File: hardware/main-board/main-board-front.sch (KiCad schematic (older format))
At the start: 25 parts, among them J5 Meter Probe, J6 Footswitch, J7 USB_A, Q1 BSS138, Q2 BSS138, Q3 BSS138, U10 USBLC6-2SC6, U11 STMPS2141, U12 USBLC6-2SC6, U9 P82B96

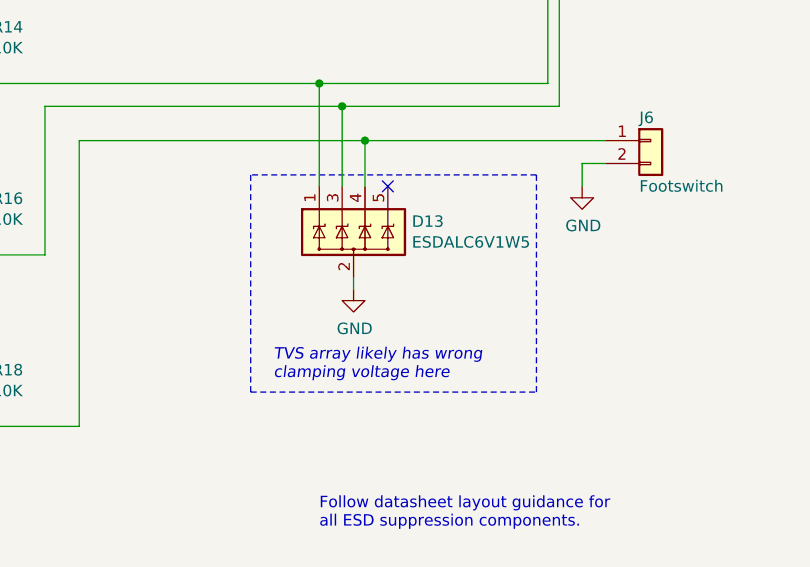
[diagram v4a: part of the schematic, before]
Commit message: Changed TVS protection on misc 5V front panel inputs
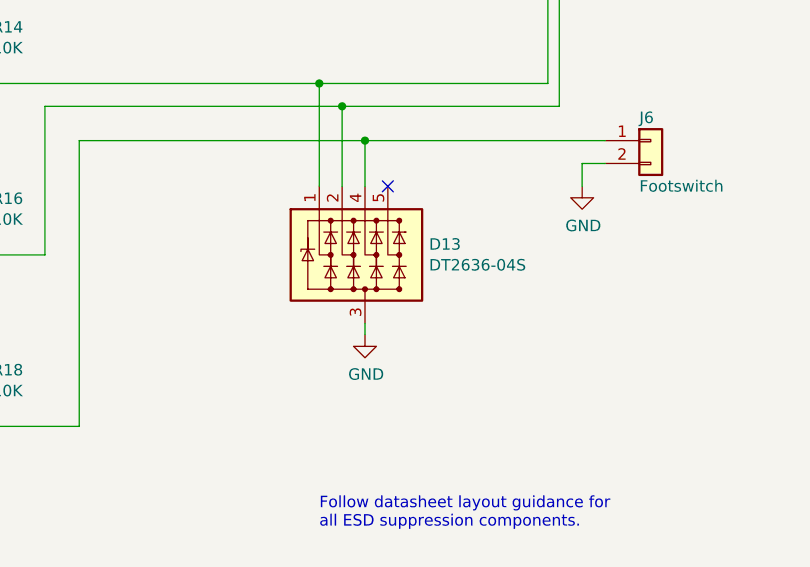
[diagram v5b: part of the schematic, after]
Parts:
- removed D13: ESDALC6V1W5, lib_fp:SOT323-5L, symbol Project:ESDALC6V1W5
- added D13: DT2636-04S, Package_TO_SOT_SMD:SOT-363_SC-70-6, symbol Project:DT2636-04S
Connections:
- net GND: now also D13.3 (GND)
- net at J6.1 (Pin_1), Q3.3 (D), R18.2: now also D13.4 (CH3)
- net at J5.6, Q1.3 (D), R14.2: now also D13.1 (CH1)
- net at J5.2, Q2.3 (D), R16.2: now also D13.2 (CH2)
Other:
- note removed: "TVS array likely has wrong\nclamping voltage here"
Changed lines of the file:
@@
 Connection ~ 2800 4150
-$Comp
-L Project:ESDALC6V1W5 D13
-U 1 1 5F9DF2EA
-P 5150 3300
-F 0 "D13" V 5104 3555 50  0000 L CNN
-F 1 "ESDALC6V1W5" V 5195 3555 50  0000 L CNN
-F 2 "lib_fp:SOT323-5L" H 5150 2925 50  0001 C CNN
-F 3 "https://www.st.com/content/ccc/resource/technical/document/datasheet/32/30/02/e6/ac/0f/46/c2/CD00002946.pdf/files/CD00002946.pdf/jcr:content/translations/en.CD00002946.pdf" H 5150 3350 50  0001 C CNN
-F 4 "TVS DIODE 3V SOT323-5" H 5150 3300 50  0001 C CNN "Description"
-F 5 "STMicroelectronics" H 5150 3300 50  0001 C CNN "Manufacturer"
-F 6 "ESDALC6V1W5" H 5150 3300 50  0001 C CNN "Manufacturer PN"
-F 7 "Digi-Key" H 5150 3300 50  0001 C CNN "Supplier"
-F 8 "497-7231-1-ND" H 5150 3300 50  0001 C CNN "Supplier PN"
-	1    5150 3300
-	0    1    1    0
-$EndComp
 $Comp
 L Power_Protection:USBLC6-2SC6 U?
@@
 L power:GND #PWR?
 U 1 1 5FA61E9F
-P 5150 3550
+P 5200 3750
 AR Path="/5FA61E9F" Ref="#PWR?"  Part="1"
 AR Path="/5FA19AFF/5FA61E9F" Ref="#PWR072"  Part="1"
-F 0 "#PWR072" H 5150 3300 50  0001 C CNN
-F 1 "GND" H 5155 3377 50  0000 C CNN
-F 2 "" H 5150 3550 50  0001 C CNN
-F 3 "" H 5150 3550 50  0001 C CNN
-	1    5150 3550
+F 0 "#PWR072" H 5200 3500 50  0001 C CNN
+F 1 "GND" H 5205 3577 50  0000 C CNN
+F 2 "" H 5200 3750 50  0001 C CNN
+F 3 "" H 5200 3750 50  0001 C CNN
+	1    5200 3750
 	1    0    0    -1
 $EndComp
 Wire Wire Line
-	5150 3500 5150 3550
+	5200 3700 5200 3750
 Text HLabel 1350 1450 0    50   BiDi ~ 0
 EXT_I2C_SDA
@@
 Wire Notes Line style solid
 	7700 1175 7700 1850
-Text Notes 4800 3950 0    50   Italic 0
-TVS array likely has wrong\nclamping voltage here
-Wire Notes Line
-	4700 3050 4700 4000
-Wire Notes Line
-	4700 4000 5950 4000
-Wire Notes Line
-	5950 4000 5950 3050
-Wire Notes Line
-	5950 3050 4700 3050
+$Comp
+L Project:DT2636-04S D13
+U 1 1 5FAA8A21
+P 5200 3400
+F 0 "D13" H 5480 3446 50  0000 L CNN
+F 1 "DT2636-04S" H 5480 3355 50  0000 L CNN
+F 2 "Package_TO_SOT_SMD:SOT-363_SC-70-6" H 5500 3350 50  0001 L CNN
+F 3 "https://www.diodes.com/assets/Datasheets/DT2636-04S.pdf" H 5525 3075 50  0001 C CNN
+F 4 "TVS DIODE 5.5V 9V SOT363" H 5200 3400 50  0001 C CNN "Description"
+F 5 "Diodes Incorporated" H 5200 3400 50  0001 C CNN "Manufacturer"
+F 6 "DT2636-04S-7" H 5200 3400 50  0001 C CNN "Manufacturer PN"
+F 7 "Digi-Key" H 5200 3400 50  0001 C CNN "Supplier"
+F 8 "DT2636-04S-7DICT-ND" H 5200 3400 50  0001 C CNN "Supplier PN"
+	1    5200 3400
+	1    0    0    -1
+$EndComp
 $EndSCHEMATC

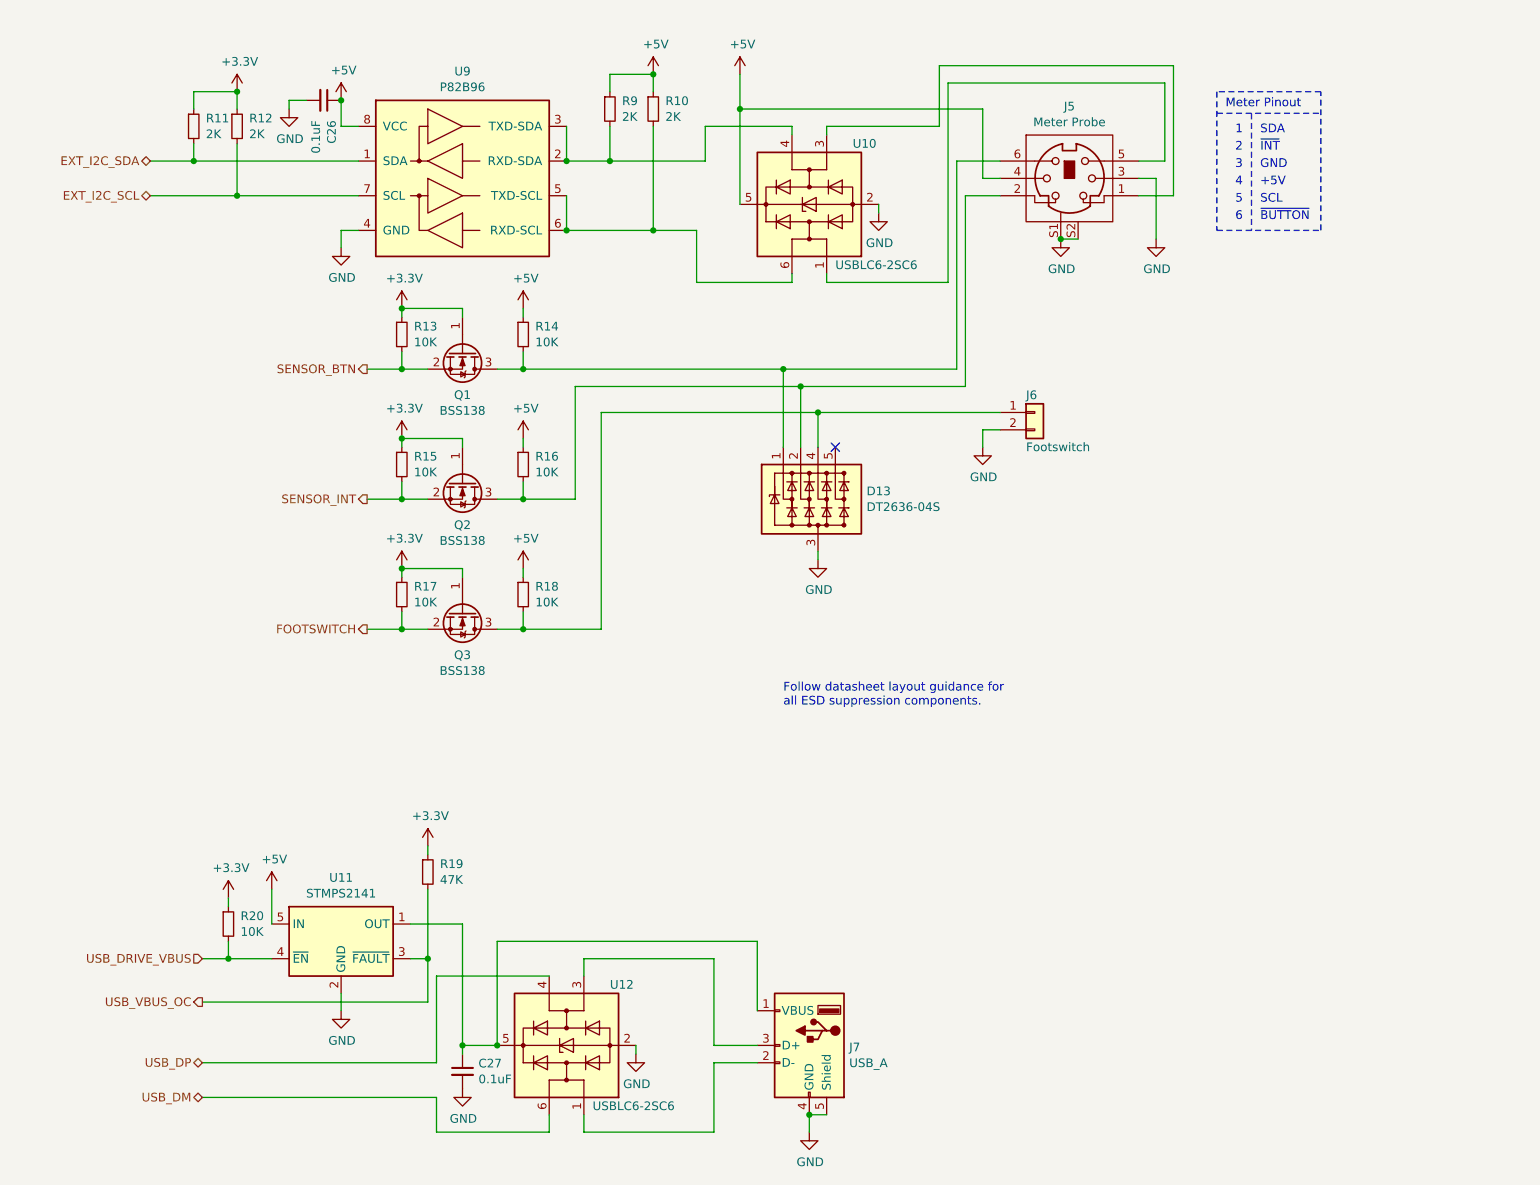
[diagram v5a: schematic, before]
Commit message: Main board schematic cleanup pass
Added mounting holes for the board and the OLED module
Connected GND and Earth nets
Cleaned up and labeled many parts of the schematic
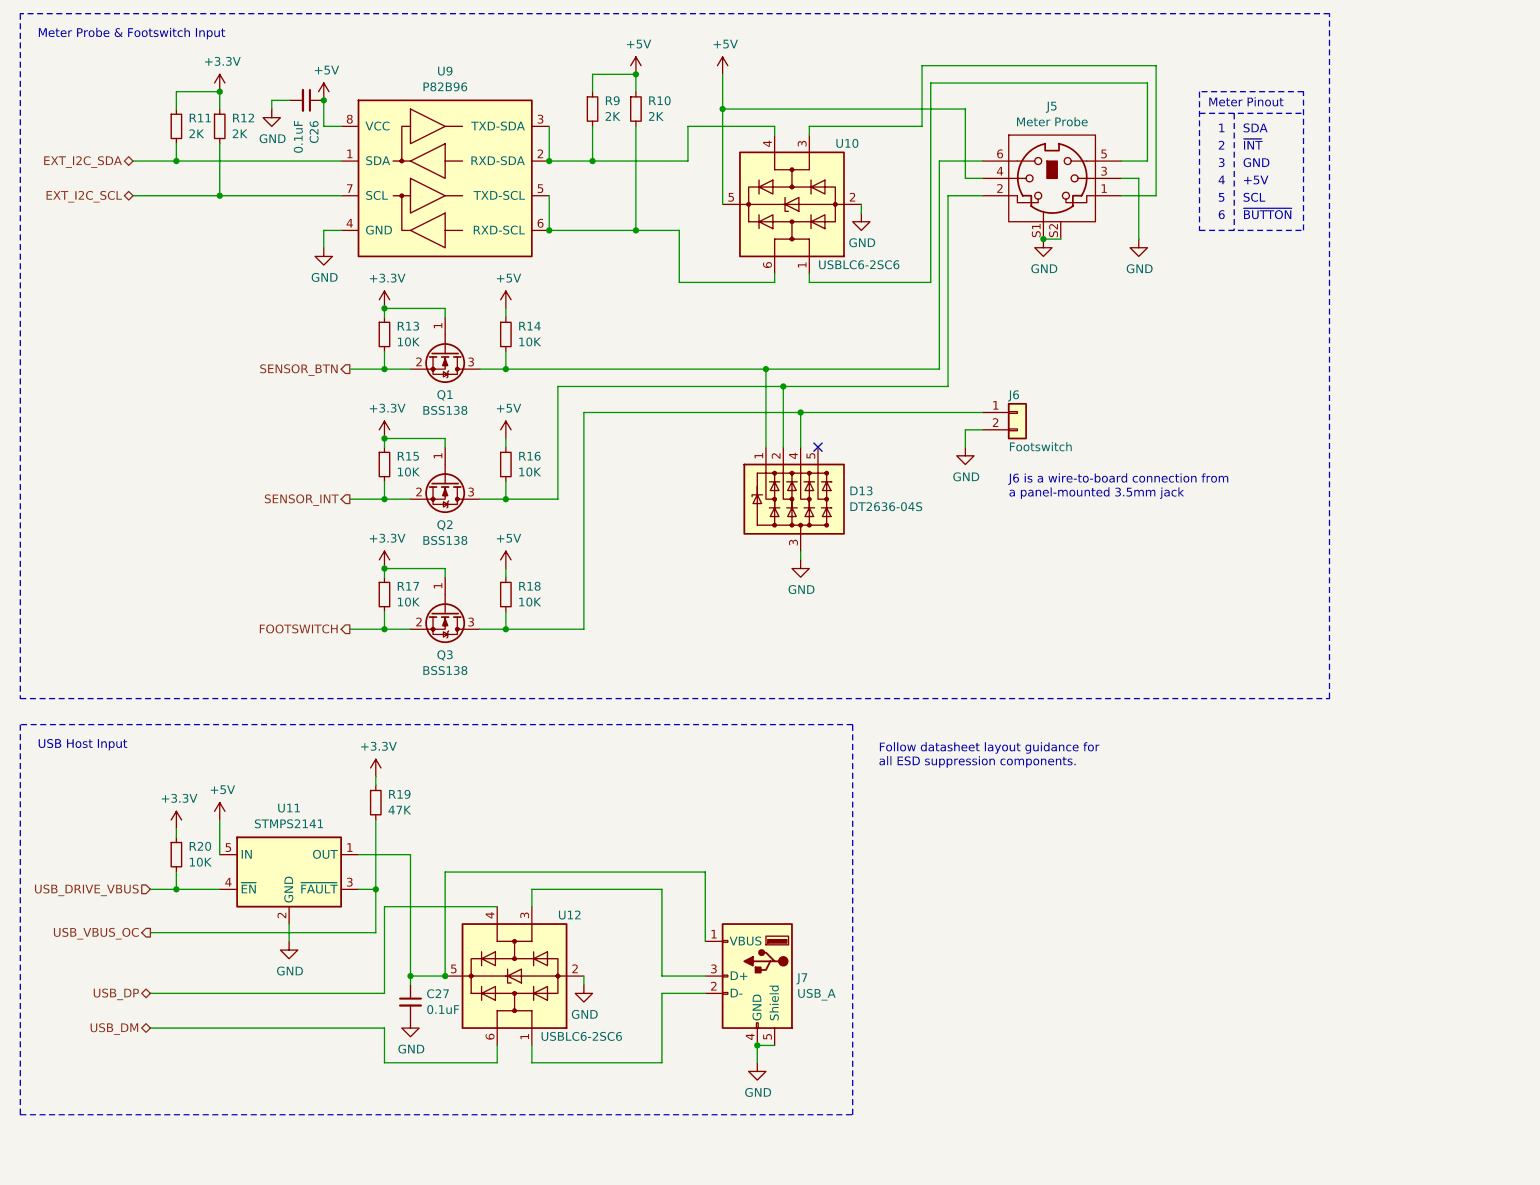
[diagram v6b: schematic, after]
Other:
- note added: "J6 is a wire-to-board connection from\na panel-mounted 3.5mm jack"
- note added: "Meter Probe & Footswitch Input"
- note added: "USB Host Input"
- moved on the sheet: C26, C27, D13, J5, J6, J7, Q1, Q2, Q3, R10, R11, R12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

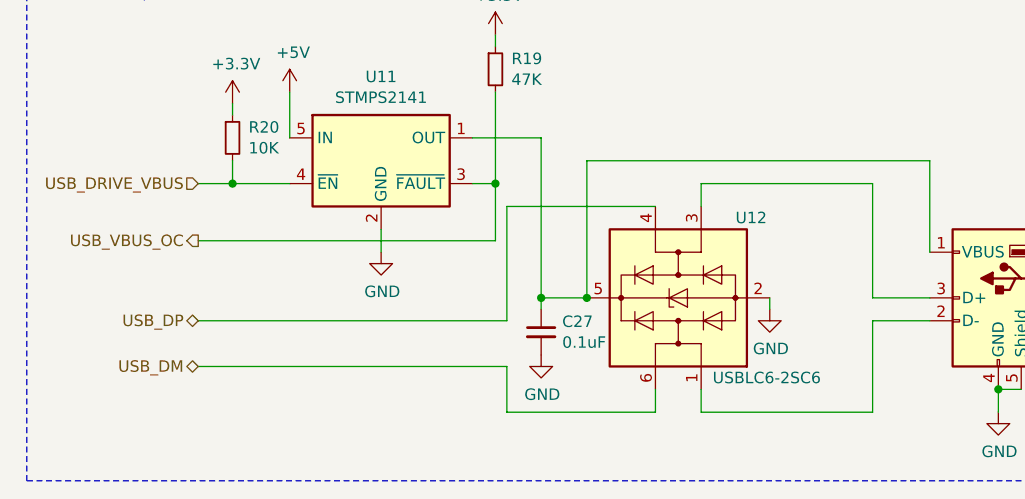
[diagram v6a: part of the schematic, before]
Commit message: Renamed USB nets so KiCad will recognize them correctly for routing
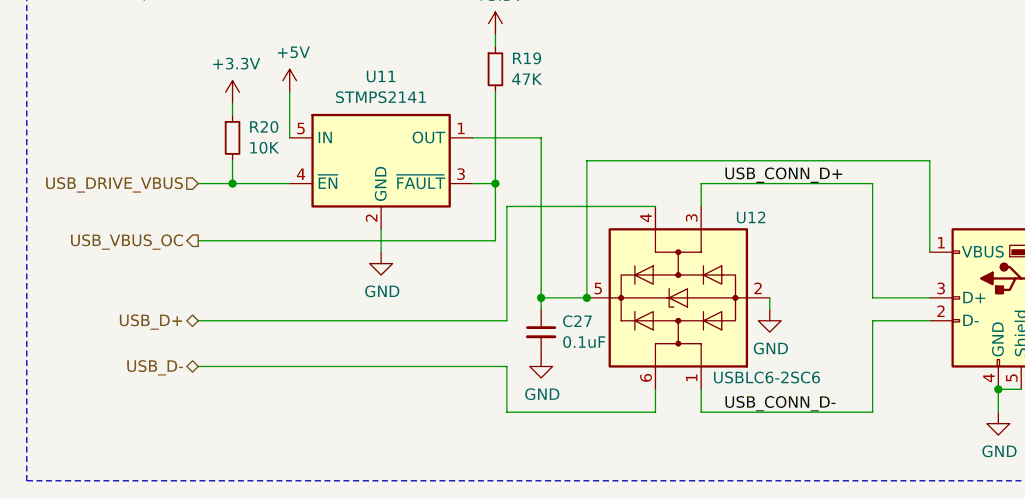
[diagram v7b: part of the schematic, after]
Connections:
- net USB_CONN_D-: now reaches J7.2 (D-), U12.1 (I/O1)
- net USB_CONN_D+: now reaches J7.3 (D+), U12.3 (I/O2)
- net USB_DM renamed USB_D-
- net USB_DP renamed USB_D+
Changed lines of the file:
@@
 USB_VBUS_OC
 Text HLabel 1350 6250 0    50   BiDi ~ 0
-USB_DP
+USB_D+
 Text HLabel 1350 6450 0    50   BiDi ~ 0
-USB_DM
+USB_D-
 Text Notes 7450 1150 0    50   ~ 0
 Meter Pinout
@@
 Wire Notes Line
 	5400 4700 600  4700
+Text Label 3650 5650 0    50   ~ 0
+USB_CONN_D+
+Text Label 3650 6650 0    50   ~ 0
+USB_CONN_D-
 $EndSCHEMATC

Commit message: Schematic cleanup
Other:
- note added: "Follow datasheet layout guidance for\nall ESD suppression components"
- note added: "J6 is a connector that connects to\na panel-mounted 3.5mm jack"
- note removed: "Follow datasheet layout guidance for\nall ESD suppression components."
- note removed: "J6 is a wire-to-board connection from\na panel-mounted 3.5mm jack"
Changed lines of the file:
@@
 AR Path="/5FA4F8F1" Ref="R?"  Part="1"
 AR Path="/5FA19AFF/5FA4F8F1" Ref="R10"  Part="1"
-F 0 "R10" H 4220 1196 50  0000 L CNN
-F 1 "2K" H 4220 1105 50  0000 L CNN
+F 0 "R10" H 4200 1200 50  0000 L CNN
+F 1 "2K" H 4200 1100 50  0000 L CNN
 F 2 "Resistor_SMD:R_0603_1608Metric" V 4080 1150 50  0001 C CNN
 F 3 "https://www.vishay.com/docs/20035/dcrcwe3.pdf" H 4150 1150 50  0001 C CNN
@@
 AR Path="/5FA4F8F7" Ref="R?"  Part="1"
 AR Path="/5FA19AFF/5FA4F8F7" Ref="R9"  Part="1"
-F 0 "R9" H 3970 1196 50  0000 L CNN
-F 1 "2K" H 3970 1105 50  0000 L CNN
+F 0 "R9" H 3950 1200 50  0000 L CNN
+F 1 "2K" H 3950 1100 50  0000 L CNN
 F 2 "Resistor_SMD:R_0603_1608Metric" V 3830 1150 50  0001 C CNN
 F 3 "https://www.vishay.com/docs/20035/dcrcwe3.pdf" H 3900 1150 50  0001 C CNN
@@
 AR Path="/5FA4F911" Ref="C?"  Part="1"
 AR Path="/5FA19AFF/5FA4F911" Ref="C26"  Part="1"
-F 0 "C26" H 2365 1146 50  0000 L CNN
-F 1 "0.1uF" H 2365 1055 50  0000 L CNN
+F 0 "C26" H 2350 1150 50  0000 L CNN
+F 1 "0.1uF" H 2350 1050 50  0000 L CNN
 F 2 "Capacitor_SMD:C_0603_1608Metric" H 2288 950 50  0001 C CNN
 F 3 "https://media.digikey.com/pdf/Data%20Sheets/Samsung%20PDFs/CL_Series_MLCC_ds.pdf" H 2250 1100 50  0001 C CNN
@@
 AR Path="/5FA4F924" Ref="R?"  Part="1"
 AR Path="/5FA19AFF/5FA4F924" Ref="R12"  Part="1"
-F 0 "R12" H 1820 1296 50  0000 L CNN
-F 1 "2K" H 1820 1205 50  0000 L CNN
+F 0 "R12" H 1800 1300 50  0000 L CNN
+F 1 "2K" H 1800 1200 50  0000 L CNN
 F 2 "Resistor_SMD:R_0603_1608Metric" V 1680 1250 50  0001 C CNN
 F 3 "https://www.vishay.com/docs/20035/dcrcwe3.pdf" H 1750 1250 50  0001 C CNN
@@
 AR Path="/5FA4F92A" Ref="R?"  Part="1"
 AR Path="/5FA19AFF/5FA4F92A" Ref="R11"  Part="1"
-F 0 "R11" H 1570 1296 50  0000 L CNN
-F 1 "2K" H 1570 1205 50  0000 L CNN
+F 0 "R11" H 1550 1300 50  0000 L CNN
+F 1 "2K" H 1550 1200 50  0000 L CNN
 F 2 "Resistor_SMD:R_0603_1608Metric" V 1430 1250 50  0001 C CNN
 F 3 "https://www.vishay.com/docs/20035/dcrcwe3.pdf" H 1500 1250 50  0001 C CNN
@@
 AR Path="/5FA5B3D0" Ref="U?"  Part="1"
 AR Path="/5FA19AFF/5FA5B3D0" Ref="U12"  Part="1"
-F 0 "U12" V 3800 5900 50  0000 R CNN
+F 0 "U12" V 3800 6500 50  0000 R CNN
 F 1 "USBLC6-2SC6" V 3100 6000 50  0000 R CNN
 F 2 "Package_TO_SOT_SMD:SOT-23-6" H 3450 5650 50  0001 C CNN
@@
 AR Path="/5FA5B3DC" Ref="J?"  Part="1"
 AR Path="/5FA19AFF/5FA5B3DC" Ref="J7"  Part="1"
-F 0 "J7" H 4620 6139 50  0000 R CNN
-F 1 "USB_A" H 4620 6048 50  0000 R CNN
+F 0 "J7" H 4900 6600 50  0000 R CNN
+F 1 "USB_A" H 4950 6500 50  0000 R CNN
 F 2 "Connector_USB:USB_A_Molex_67643_Horizontal" H 5000 6100 50  0001 C CNN
 F 3 "https://www.molex.com/pdm_docs/sd/676430910_sd.pdf" H 5000 6100 50  0001 C CNN
@@
 Connection ~ 4850 6550
 Text Notes 5550 4950 0    50   ~ 0
-Follow datasheet layout guidance for\nall ESD suppression components.
+Follow datasheet layout guidance for\nall ESD suppression components
 Wire Wire Line
 	2550 5450 2850 5450
@@
 Connection ~ 2850 6150
 Wire Wire Line
-	3350 5750 2700 5750
-Wire Wire Line
-	2700 5750 2700 6250
+	2700 5650 2700 6250
 Wire Wire Line
 	2700 6250 1350 6250
@@
 U 1 1 5F988495
 P 2850 6300
-F 0 "C27" H 2942 6346 50  0000 L CNN
-F 1 "0.1uF" H 2942 6255 50  0000 L CNN
+F 0 "C27" H 2925 6325 50  0000 L CNN
+F 1 "0.1uF" H 2925 6250 50  0000 L CNN
 F 2 "Capacitor_SMD:C_0603_1608Metric" H 2850 6300 50  0001 C CNN
 F 3 "https://media.digikey.com/pdf/Data%20Sheets/Samsung%20PDFs/CL_Series_MLCC_ds.pdf" H 2850 6300 50  0001 C CNN
@@
 AR Path="/5F9E0AB3" Ref="U?"  Part="1"
 AR Path="/5FA19AFF/5F9E0AB3" Ref="U10"  Part="1"
-F 0 "U10" V 5400 1450 50  0000 R CNN
+F 0 "U10" V 5400 2050 50  0000 R CNN
 F 1 "USBLC6-2SC6" V 4700 1550 50  0000 R CNN
 F 2 "Package_TO_SOT_SMD:SOT-23-6" H 5050 1200 50  0001 C CNN
@@
 Text HLabel 1350 6450 0    50   BiDi ~ 0
 USB_D-
-Text Notes 7450 1150 0    50   ~ 0
+Text Notes 7400 1150 0    50   ~ 0
 Meter Pinout
-Text Notes 7550 1300 2    50   ~ 0
+Text Notes 7500 1300 2    50   ~ 0
 1
-Text Notes 7550 1400 2    50   ~ 0
+Text Notes 7500 1400 2    50   ~ 0
 2
-Text Notes 7550 1500 2    50   ~ 0
+Text Notes 7500 1500 2    50   ~ 0
 3
-Text Notes 7550 1600 2    50   ~ 0
+Text Notes 7500 1600 2    50   ~ 0
 4
-Text Notes 7550 1700 2    50   ~ 0
+Text Notes 7500 1700 2    50   ~ 0
 5
-Text Notes 7550 1800 2    50   ~ 0
+Text Notes 7500 1800 2    50   ~ 0
 6
-Text Notes 7650 1300 0    50   ~ 0
+Text Notes 7600 1300 0    50   ~ 0
 SDA
-Text Notes 7650 1400 0    50   ~ 0
+Text Notes 7600 1400 0    50   ~ 0
 ~INT
-Text Notes 7650 1500 0    50   ~ 0
+Text Notes 7600 1500 0    50   ~ 0
 GND
-Text Notes 7650 1600 0    50   ~ 0
+Text Notes 7600 1600 0    50   ~ 0
 +5V
-Text Notes 7650 1700 0    50   ~ 0
+Text Notes 7600 1700 0    50   ~ 0
 SCL
-Text Notes 7650 1800 0    50   ~ 0
+Text Notes 7600 1800 0    50   ~ 0
 ~BUTTON
 Wire Notes Line style solid
-	7400 1050 7400 1850
+	7350 1050 7350 1850
 Wire Notes Line style solid
-	7400 1850 8000 1850
+	7350 1850 7950 1850
 Wire Notes Line style solid
-	8000 1850 8000 1050
+	7950 1850 7950 1050
 Wire Notes Line style solid
-	8000 1050 7400 1050
+	7950 1050 7350 1050
 Wire Notes Line style solid
-	7400 1175 8000 1175
+	7350 1175 7950 1175
 Wire Notes Line style solid
-	7600 1175 7600 1850
+	7550 1175 7550 1850
 $Comp
 L Project:DT2636-04S D13
@@
 $EndComp
 Text Notes 6300 3400 0    50   ~ 0
-J6 is a wire-to-board connection from\na panel-mounted 3.5mm jack
+J6 is a connector that connects to\na panel-mounted 3.5mm jack
 Text Notes 700  750  0    50   ~ 0
 Meter Probe & Footswitch Input
@@
 Text Label 3650 6650 0    50   ~ 0
 USB_CONN_D-
+Wire Wire Line
+	2700 5650 3350 5650
+Wire Wire Line
+	3350 5650 3350 5750
 $EndSCHEMATC
